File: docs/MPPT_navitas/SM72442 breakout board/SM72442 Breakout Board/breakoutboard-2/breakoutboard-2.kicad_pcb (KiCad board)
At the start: 2 copper layers, 113 parts, among them J1 PV_IN, J10 10V, J2 Connector_Generic_Conn_01x02, J3 Iin_sense_INA, J4 Iout_sense_INA, J5 Iin_sense, J6 PV, J7 BAT, J8 Iout_sense, J9 Vout, J9-1 Connector_Generic_Conn_01x05, Q3 2N7002, Q4 2N7002, Q5 2N7002, Q6 2N7002, U10 Driver_FET_SM72295MA_Navitas, U12 INA199A1DCKR_NAVITAS, U13 INA199A1DCKR_NAVITAS

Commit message: update on pcb (in progress)
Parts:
- added J11: 5V_conn, Connector_PinSocket_2.00mm:PinSocket_1x01_P2.00mm_Vertical, F.Cu at (60.1, 178.3)
- moved C82 130.8 mm to (203.2, 40.0), turned to 90 degrees
- moved C53 124.8 mm to (104.8, 39.1), turned to 90 degrees
- moved C74 124.2 mm to (197.1, 40.0), turned to 90 degrees
- moved C61 123.5 mm to (188.0, 40.0), turned to 90 degrees
- moved C50 120.7 mm to (215.0, 50.5)
- moved C65 120.5 mm to (112.4, 39.1), turned to 90 degrees
- moved R59 119.6 mm to (89.8, 48.0)
- moved C69 117.5 mm to (115.4, 39.1), turned to 90 degrees
- moved C71 117.5 mm to (117.0, 39.1), turned to 90 degrees
- moved D13 112.3 mm to (180.8, 71.9)
- moved R61 108.3 mm to (95.2, 52.2)
- moved R70 102.7 mm to (188.3, 71.1)
- moved D20 101.3 mm to (180.8, 81.4)
- moved C47 101.1 mm to (83.4, 51.9)
- moved C78 98.2 mm to (200.2, 40.0), turned to 90 degrees
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
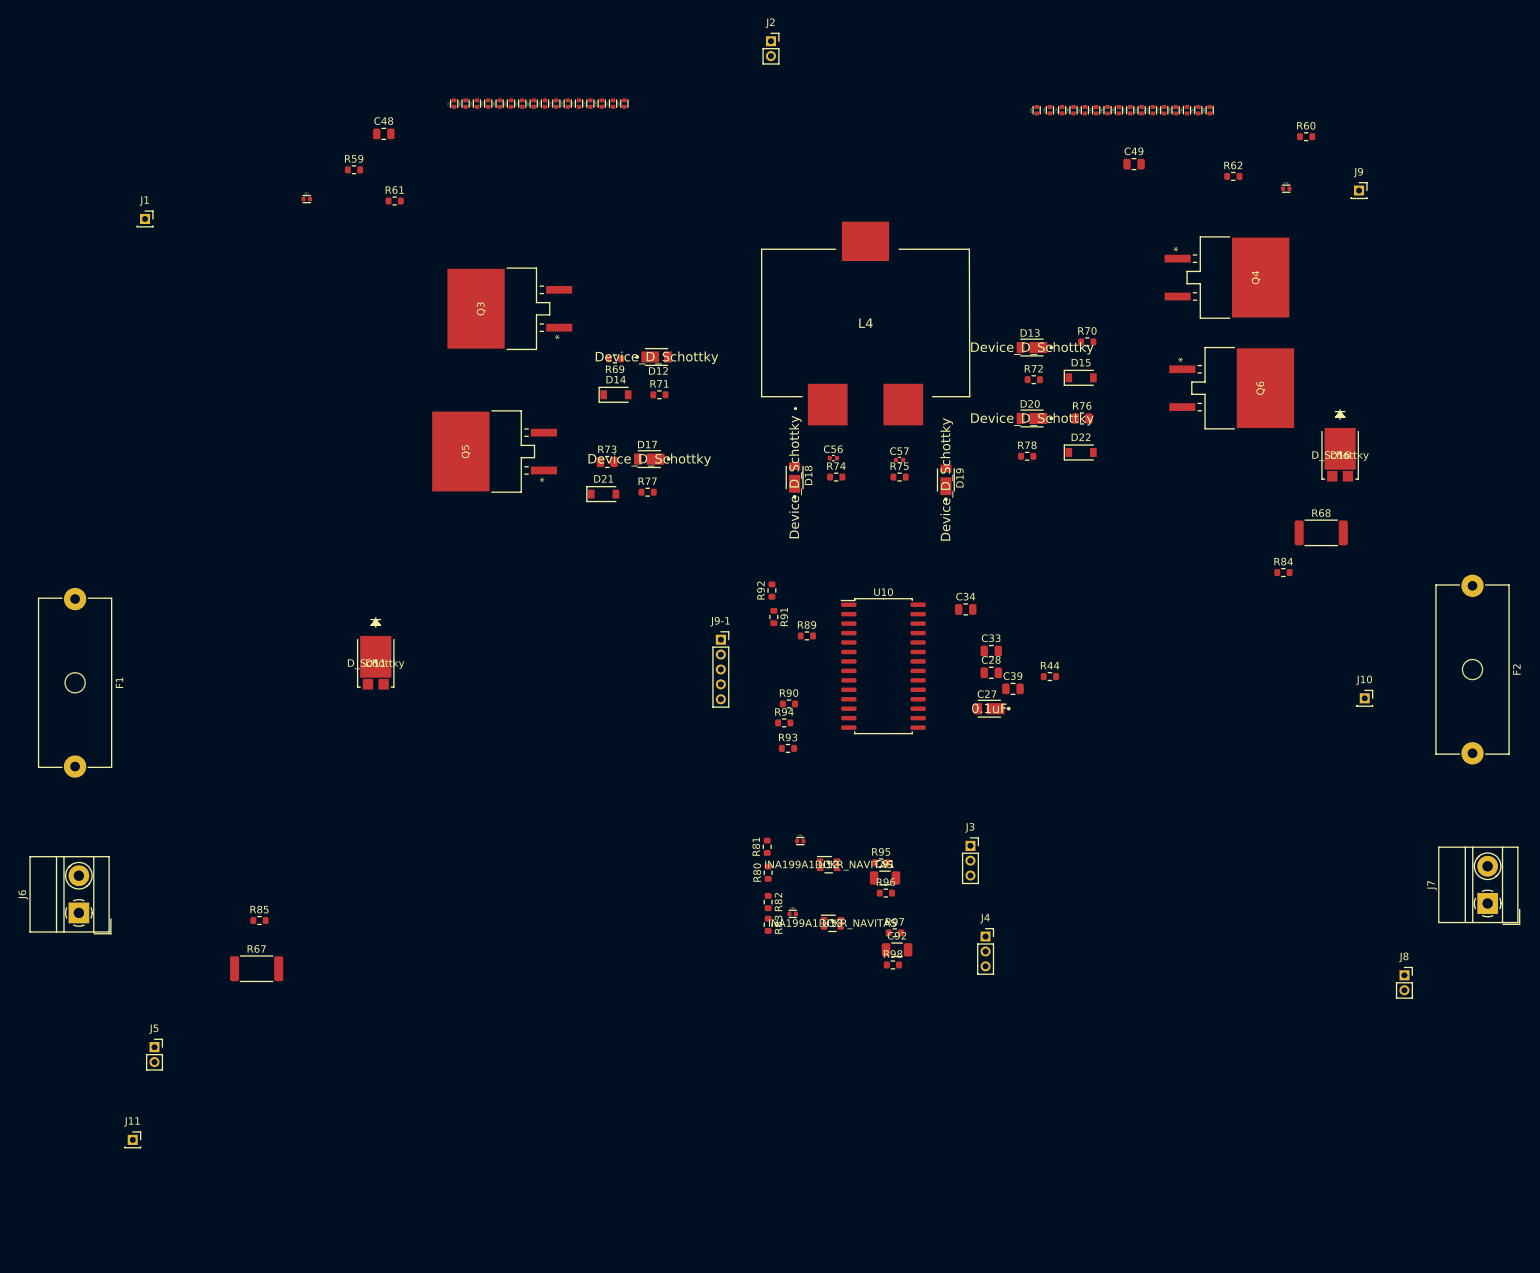
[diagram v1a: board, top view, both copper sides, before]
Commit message: PCB layout updated, next step to make traces & dimensions
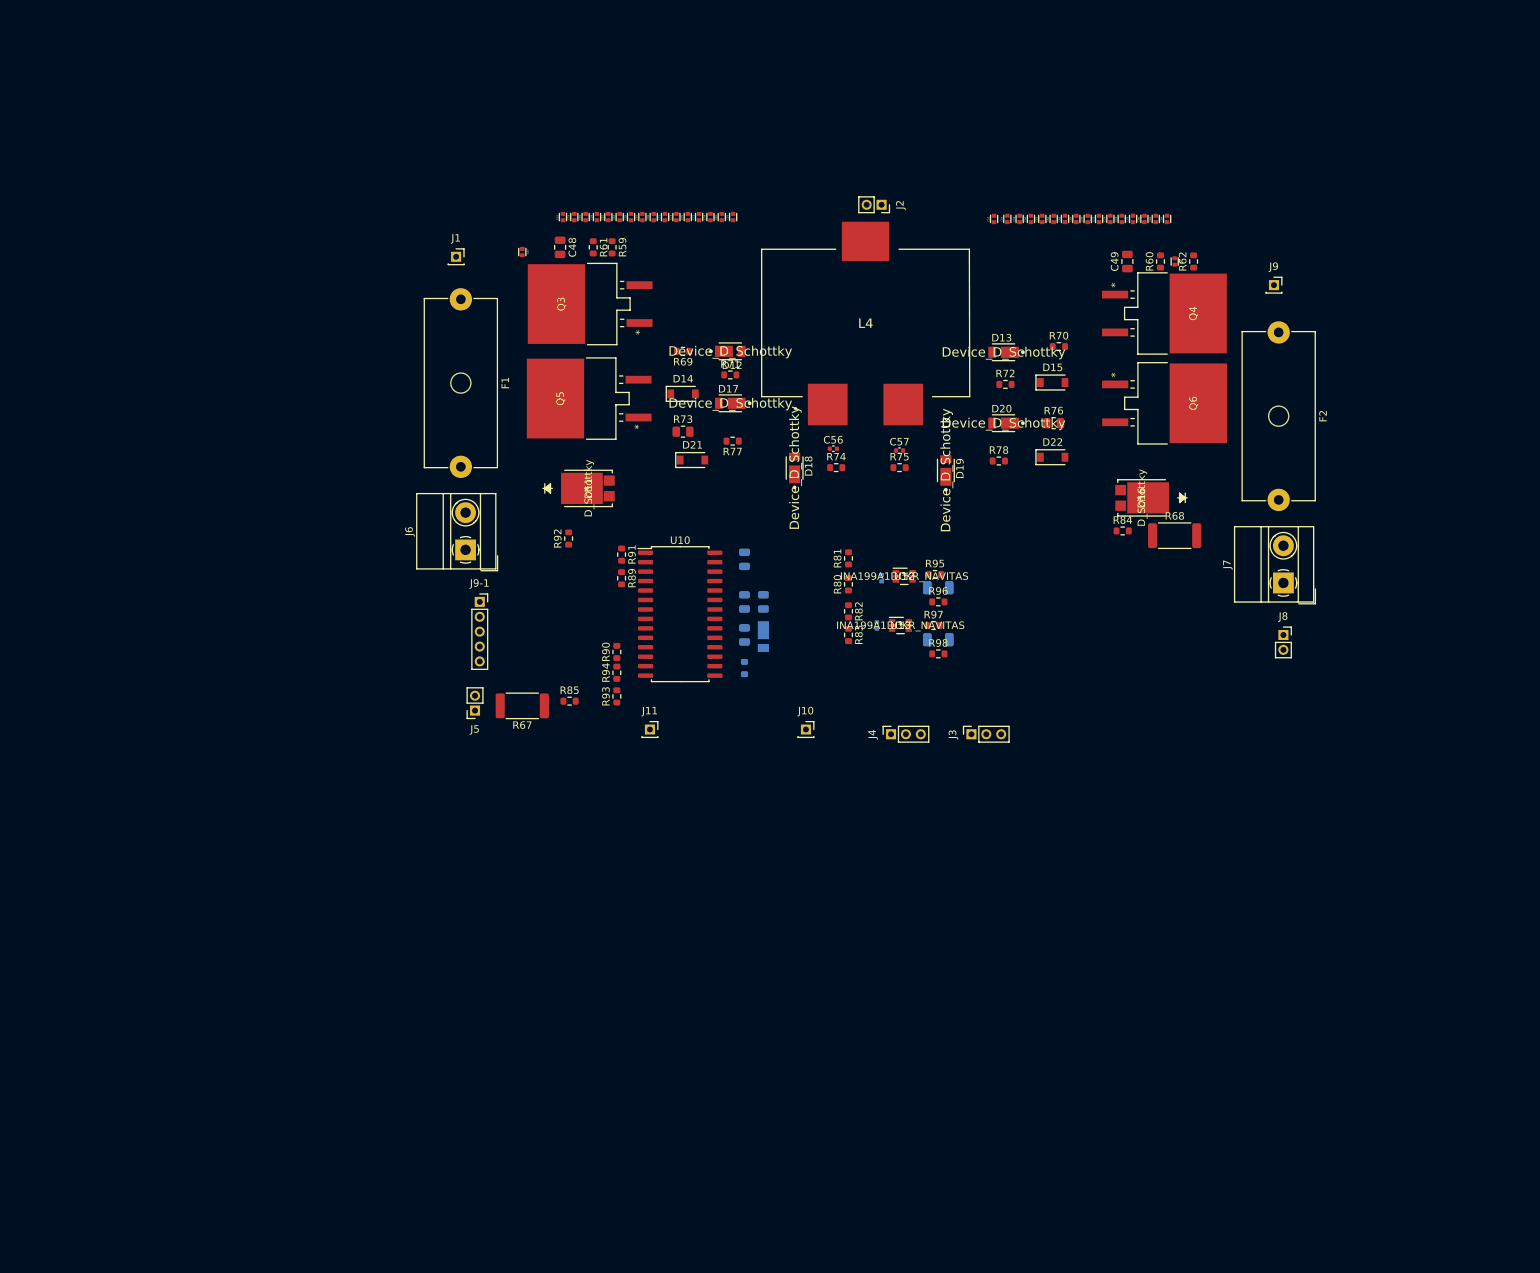
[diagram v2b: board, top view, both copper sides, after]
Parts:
- C27, C28, C33, C34, C39, C89, C91, C92, C99, R44: moved to B.Cu
- moved J11 88.7 mm to (129.5, 123.2)
- moved J10 75.2 mm to (150.5, 123.2)
- moved J6 71.2 mm to (104.8, 99.1)
- moved F1 65.6 mm to (104.1, 65.4)
- moved J5 62.4 mm to (106.0, 120.7), turned to 180 degrees
- moved J7 51.0 mm to (214.6, 103.5)
- moved R85 51.0 mm to (118.7, 119.4)
- moved R67 50.2 mm to (112.4, 120.0), turned to 180 degrees
- moved J8 48.5 mm to (214.6, 110.5)
- moved F2 42.9 mm to (214.0, 69.8)
- moved R98 42.2 mm to (168.3, 113.0)
- moved J1 42.1 mm to (103.5, 59.7)
- moved C92 42.0 mm to (168.3, 111.1)
- moved R97 41.6 mm to (167.6, 109.2)
- moved R44 41.0 mm to (142.2, 114.9), turned to 270 degrees
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
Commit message: PCB update
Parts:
- C34: moved to F.Cu
- moved J3 30.4 mm to (187.3, 97.2), turned to 0 degrees
- moved J9-1 17.1 mm to (118.7, 118.1), turned to 90 degrees
- moved R85 16.6 mm to (117.5, 102.9)
- moved R67 15.5 mm to (107.3, 105.4)
- moved R68 11.9 mm to (203.2, 108.6)
- moved R97 11.8 mm to (178.2, 104.1)
- moved R84 11.6 mm to (194.9, 108.0), turned to 180 degrees
- moved R90 11.5 mm to (135.3, 107.3)
- moved C27 11.4 mm to (154.9, 105.6)
- moved C28 11.4 mm to (154.9, 101.0)
- moved C33 11.4 mm to (152.4, 101.0)
- moved C34 11.4 mm to (152.4, 95.2)
- moved C39 11.4 mm to (152.4, 105.4)
- moved C89 11.4 mm to (170.8, 97.8)
- moved C91 11.4 mm to (178.4, 99.1)
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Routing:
- net GND: track 0.00 -> 168.5 mm, vias 0 -> 8
- net Net-(C47-Pad2): track 0.00 -> 131.8 mm, vias 0 -> 2
- net Net-(C50-Pad2): track 0.00 -> 130.7 mm, vias 0 -> 2
- net HSB: track 0.00 -> 103.2 mm, vias 0 -> 2
- net HSA: track 0.00 -> 77.9 mm
- net HOB: track 0.00 -> 73.6 mm, vias 0 -> 2
- net +5V: track 0.00 -> 56.0 mm, vias 0 -> 6
- net Vout_Sense: track 0.00 -> 46.7 mm
- net LOB: track 0.00 -> 45.7 mm, vias 0 -> 2
- net Vin_Sense: track 0.00 -> 44.9 mm
- net Net-(C28-Pad1): track 0.00 -> 34.8 mm, vias 0 -> 3
- net Net-(J9-1-Pad1): track 0.00 -> 32.0 mm
- net HOA: track 0.00 -> 31.4 mm
- net Net-(J9-1-Pad2): track 0.00 -> 29.6 mm
- net Net-(D15-Pad2): track 0.00 -> 27.3 mm, vias 0 -> 2
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- added copper zone on B.Cu, net GND
- added copper zone on F.Cu, net GND
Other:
- board outline added: 124.5 x 71.1 mm

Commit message: MPPT PCB completed, Gerber generated
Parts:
- D11, D16: footprint fsv201:FSV10100V -> Package_TO_SOT_SMD:TO-263-2
- moved R92 7.14 mm to (123.8, 102.4)
- moved D16 5.12 mm to (198.1, 96.5), turned to 0 degrees
- moved D11 4.26 mm to (119.4, 94.6), turned to 180 degrees
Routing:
- net GND: track 168.5 -> 284.2 mm, vias 8 -> 10
- net Net-(C47-Pad2): track 131.8 -> 145.3 mm
- net (no net): track 0.00 -> 13.0 mm, vias 0 -> 3
- net Net-(D14-Pad2): track 18.1 -> 21.6 mm
- net Net-(C50-Pad2): track 130.7 -> 127.4 mm
- net Net-(R92-Pad2): track 21.5 -> 18.5 mm
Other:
- board text added: "Purdue Solar Racing MPPT Ver.1 Fan Jing Hoon - January 2022"

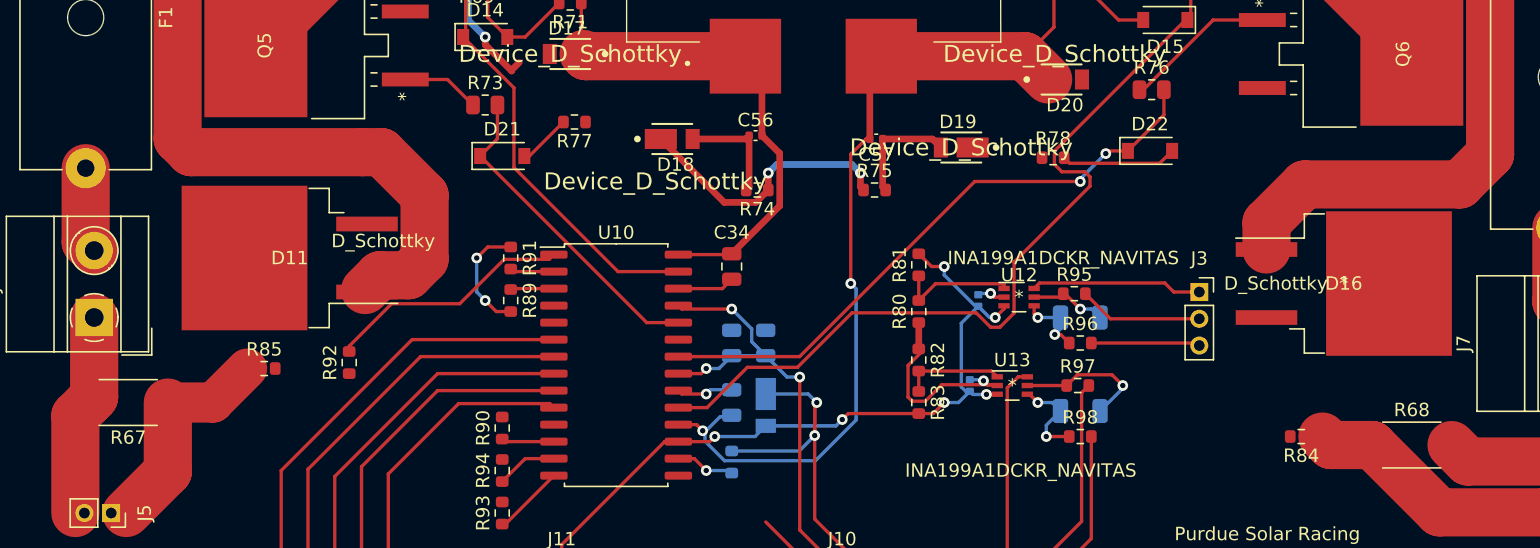
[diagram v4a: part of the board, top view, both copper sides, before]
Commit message: footprint fixed, Gerber updated
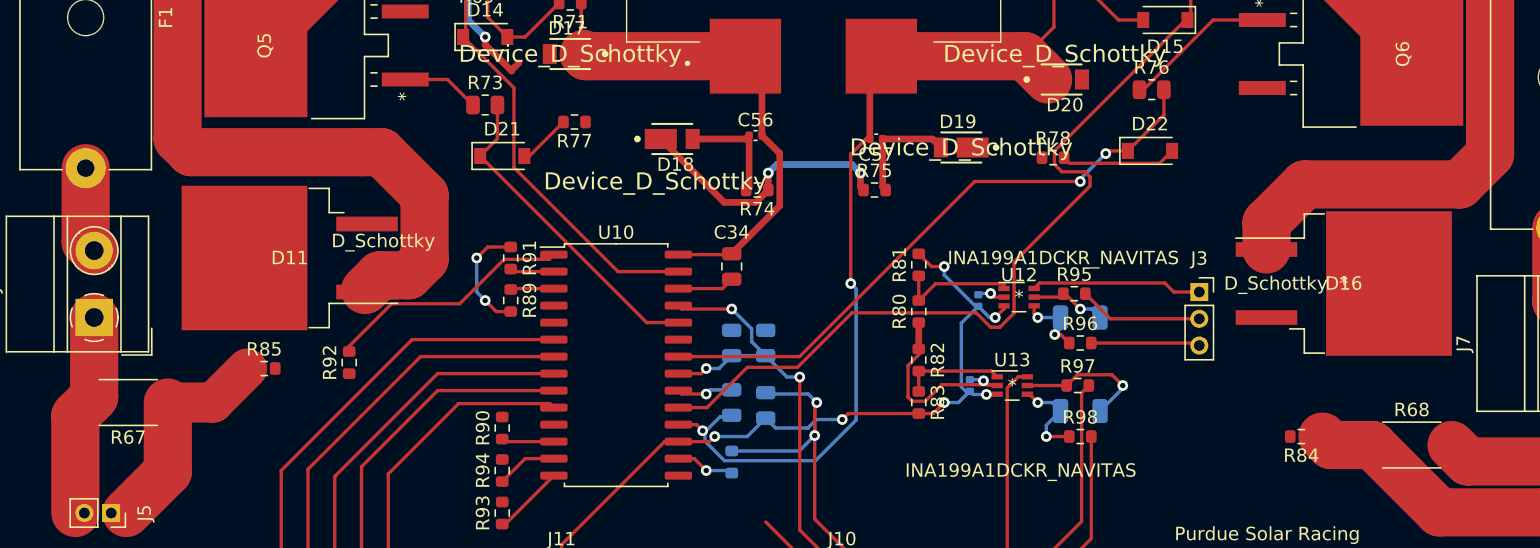
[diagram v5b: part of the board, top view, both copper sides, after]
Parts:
- C27: footprint DFLS1200-7:Diodes_Inc.-PowerDI123-03_2017-0-MFG -> Capacitor_SMD:C_0805_2012Metric
- turned C27 to 270 degrees
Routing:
- net +5V: track 56.0 -> 56.6 mm
